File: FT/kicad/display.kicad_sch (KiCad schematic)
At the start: 20 parts, among them Q1 Q_NPN_BEC, Q2 Q_NPN_BEC, Q3 Q_NPN_BEC, Q4 Q_NPN_BEC, U1 HDSP-7501, U2 HDSP-7501, U3 HDSP-7501, U4 HDSP-7501

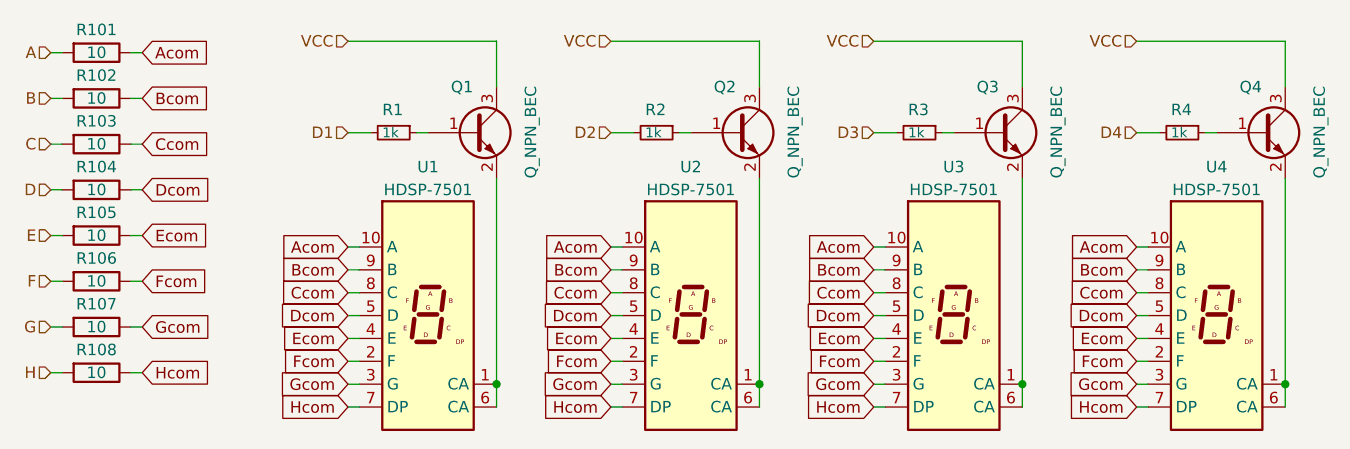
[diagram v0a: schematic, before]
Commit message: Final Task Example
npn to pnp
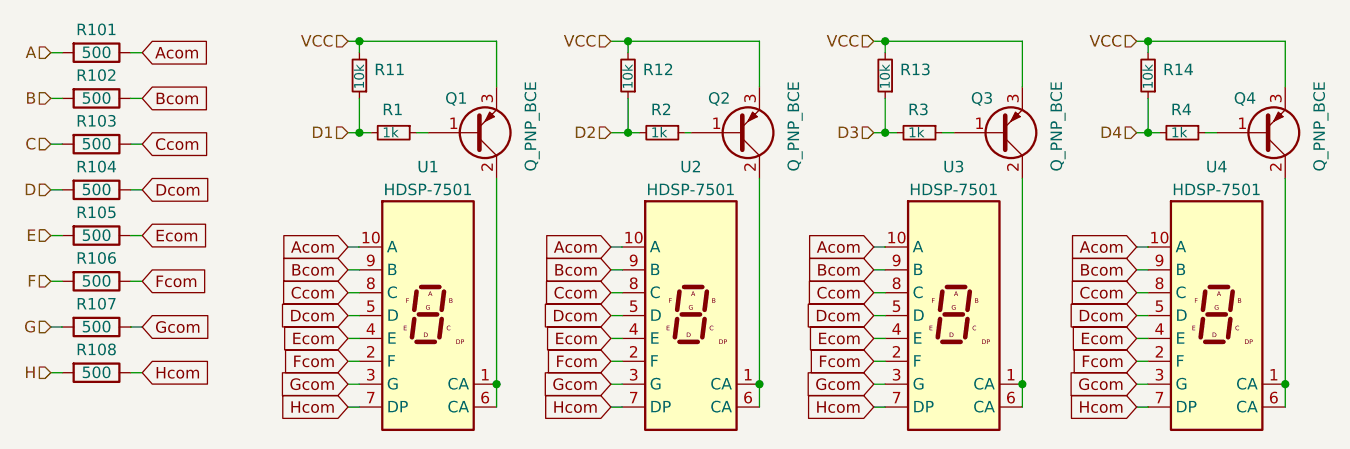
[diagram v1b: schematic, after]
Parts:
- removed Q1, Q2, Q3, Q4: Q_NPN_BEC, Package_TO_SOT_SMD:SOT-23, symbol Device:Q_NPN_BEC
- added Q1, Q2, Q3, Q4: Q_PNP_BCE, Package_TO_SOT_SMD:SOT-23, symbol Device:Q_PNP_BCE
- added R11, R12, R13, R14: 10k, Resistor_SMD:R_0603_1608Metric, symbol Device:R_Small
- R101, R102, R103, R104, R105, R106, R107, R108: value 10 -> 500
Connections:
- net D1: now also R11.1
- net D2: now also R12.1
- net D3: now also R13.1
- net D4: now also R14.1
- net VCC: now also Q1.3 (E), Q2.3 (E), Q3.3 (E), Q4.3 (E), R11.2, R12.2, R13.2, R14.2
- net at R1.1: now also Q1.1 (B)
- net at U1.1 (CA), U1.6 (CA): now also Q1.2 (C)
- net at R4.1: now also Q4.1 (B)
- net at R3.1: now also Q3.1 (B)
- net at U3.1 (CA), U3.6 (CA): now also Q3.2 (C)
- net at U2.1 (CA), U2.6 (CA): now also Q2.2 (C)
- net at R2.1: now also Q2.1 (B)
- net at U4.1 (CA), U4.6 (CA): now also Q4.2 (C)
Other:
- moved on the sheet: R2
